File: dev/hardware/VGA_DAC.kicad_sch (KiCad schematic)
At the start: 1 part, among them J201 Conn_01x08

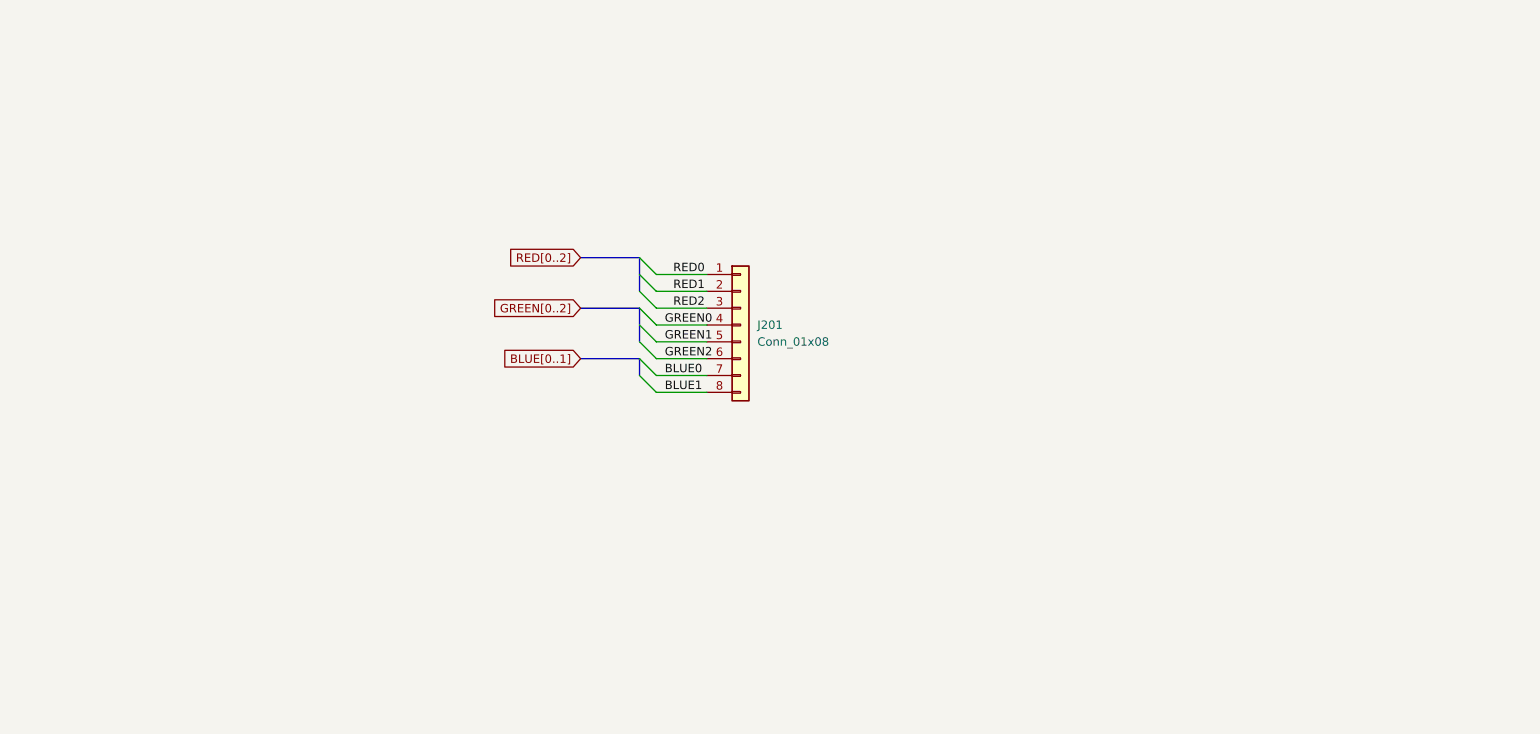
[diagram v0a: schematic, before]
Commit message: Finalized initial schematic
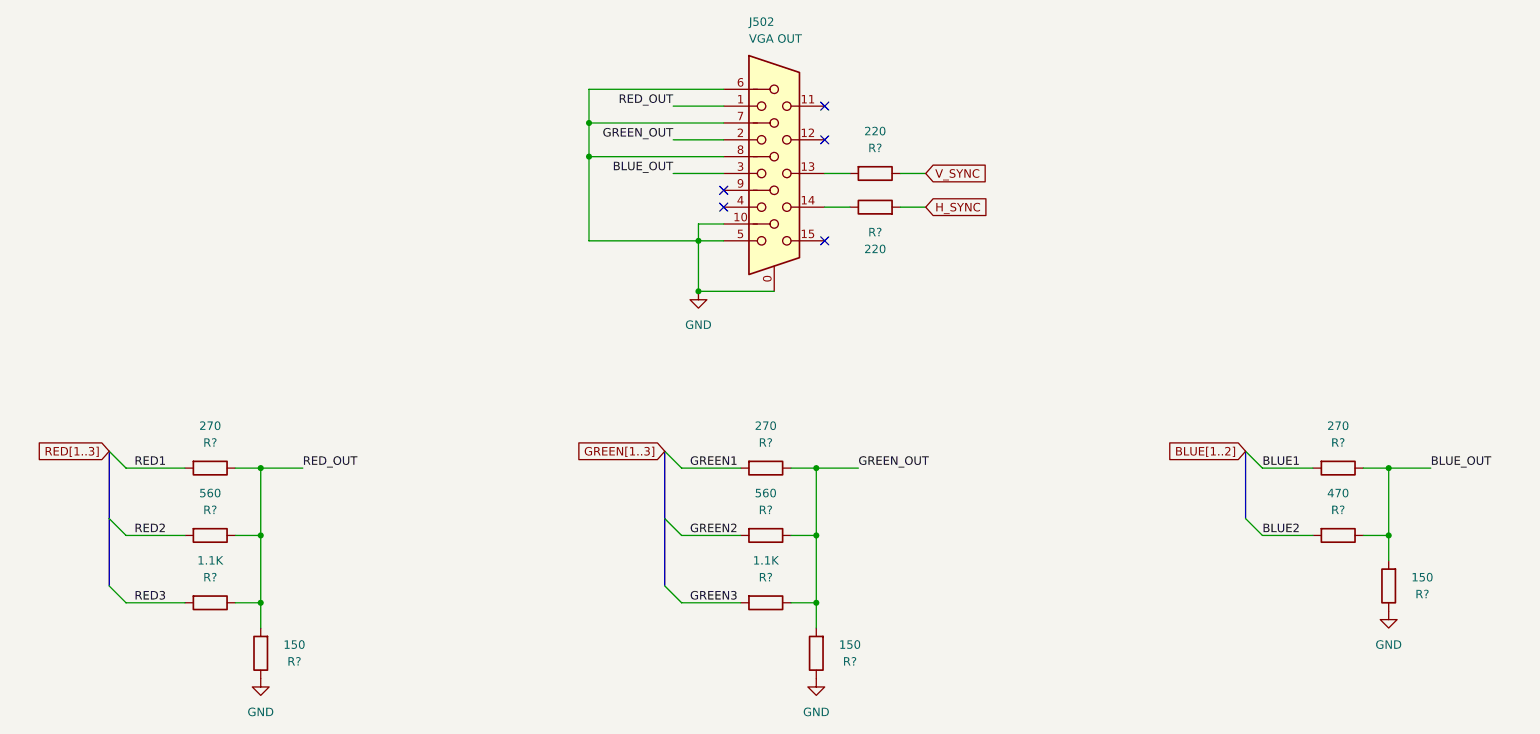
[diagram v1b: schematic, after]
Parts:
- removed J201: Conn_01x08, symbol Connector_Generic:Conn_01x08
- added J502: VGA OUT, Connector_Dsub:DSUB-15-HD_Female_Horizontal_P2.29x1.98mm_EdgePinOffset8.35mm_Housed_MountingHolesOffset10.89mm, symbol Connector:DE15_Receptacle_HighDensity_MountingHoles
- added R? (x2): 220, Resistor_THT:R_Axial_DIN0207_L6.3mm_D2.5mm_P10.16mm_Horizontal, symbol Device:R
- added R? (x2): 1.1K, Resistor_THT:R_Axial_DIN0207_L6.3mm_D2.5mm_P10.16mm_Horizontal, symbol Device:R
- added R? (x2): 560, Resistor_THT:R_Axial_DIN0207_L6.3mm_D2.5mm_P10.16mm_Horizontal, symbol Device:R
- added R?: 470, Resistor_THT:R_Axial_DIN0207_L6.3mm_D2.5mm_P10.16mm_Horizontal, symbol Device:R
- added R? (x3): 150, Resistor_THT:R_Axial_DIN0207_L6.3mm_D2.5mm_P10.16mm_Horizontal, symbol Device:R
- added R? (x3): 270, Resistor_THT:R_Axial_DIN0207_L6.3mm_D2.5mm_P10.16mm_Horizontal, symbol Device:R
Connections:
- net BLUE1: now also R?.2
- net GREEN1: now also R?.2
- net GREEN2: now also R?.2
- net RED1: now also R?.2
- net RED2: now also R?.2
- new net: J502.13, R?.2
- new net: J502.14, R?.1
- new net BLUE2: R?.2
- new net BLUE_OUT: J502.3, R?.1, R?.1, R?.2
- new net GND: J502.0, J502.10, J502.5, J502.6, J502.7, J502.8, R?.1, R?.1, R?.1
- new net GREEN3: R?.2
- new net GREEN_OUT: J502.2, R?.1, R?.1, R?.1, R?.2
- new net H_SYNC: R?.2
- new net RED3: R?.2
- new net RED_OUT: J502.1, R?.1, R?.1, R?.1, R?.2
- new net V_SYNC: R?.1
- no-connect marks 0 -> 5

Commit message: Started developing PCB layout
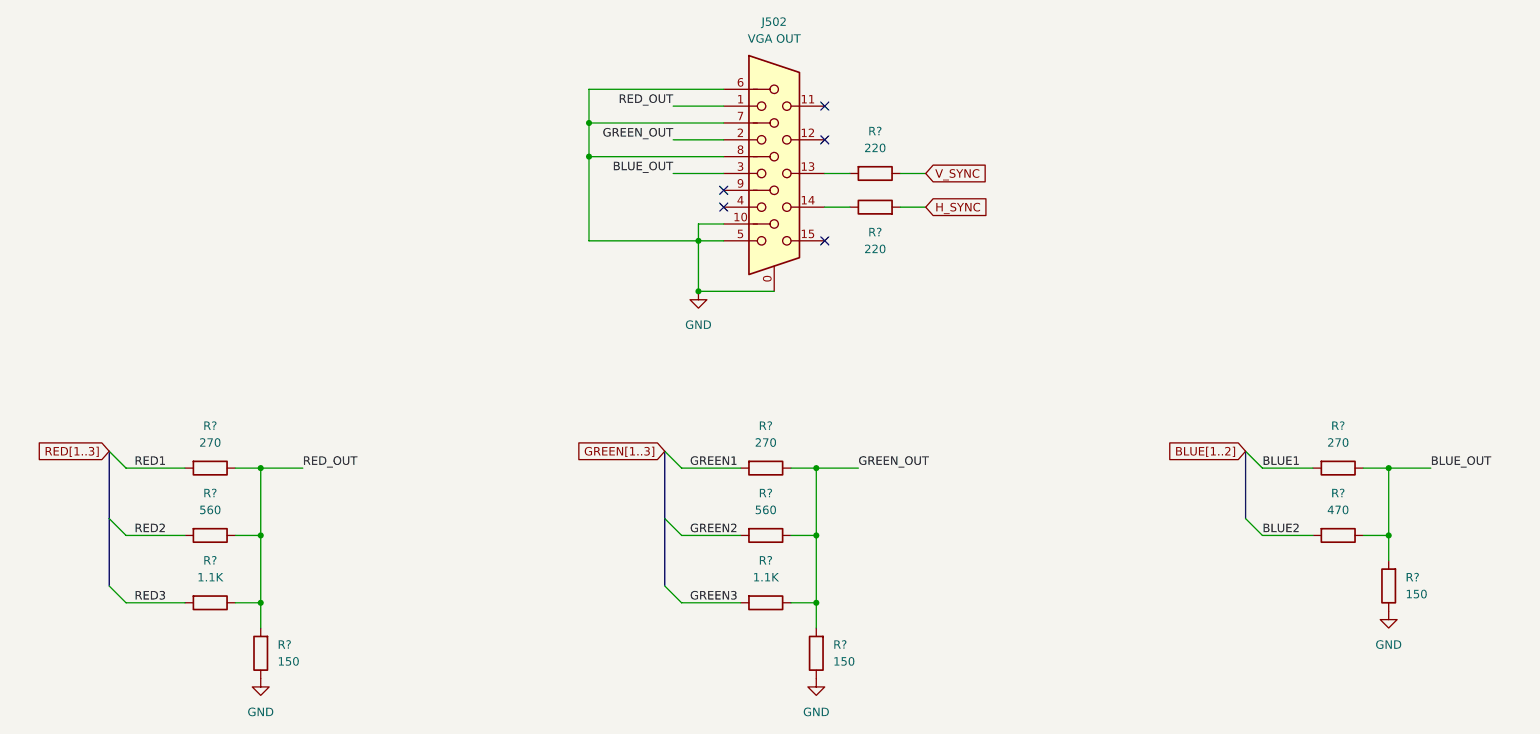
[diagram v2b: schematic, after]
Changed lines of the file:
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@@
   )
   (symbol (lib_id "Device:R") (at 161.29 63.5 270) (unit 1)
-    (in_bom yes) (on_board yes) (dnp no)
-    (property "Reference" "R?" (at 161.29 59.69 90)
-      (effects (font (size 1.27 1.27)))
-    )
-    (property "Value" "220" (at 161.29 57.15 90)
+    (in_bom yes) (on_board yes) (dnp no) (fields_autoplaced)
+    (property "Reference" "R?" (at 161.29 57.15 90)
+      (effects (font (size 1.27 1.27)))
+    )
+    (property "Value" "220" (at 161.29 59.69 90)
       (effects (font (size 1.27 1.27)))
     )
@@
   )
   (symbol (lib_id "Device:R") (at 144.78 128.27 270) (unit 1)
-    (in_bom yes) (on_board yes) (dnp no)
-    (property "Reference" "R?" (at 144.78 124.46 90)
-      (effects (font (size 1.27 1.27)))
-    )
-    (property "Value" "1.1K" (at 144.78 121.92 90)
+    (in_bom yes) (on_board yes) (dnp no) (fields_autoplaced)
+    (property "Reference" "R?" (at 144.78 121.92 90)
+      (effects (font (size 1.27 1.27)))
+    )
+    (property "Value" "1.1K" (at 144.78 124.46 90)
       (effects (font (size 1.27 1.27)))
     )
@@
   )
   (symbol (lib_id "Device:R") (at 60.96 118.11 270) (unit 1)
-    (in_bom yes) (on_board yes) (dnp no)
-    (property "Reference" "R?" (at 60.96 114.3 90)
-      (effects (font (size 1.27 1.27)))
-    )
-    (property "Value" "560" (at 60.96 111.76 90)
+    (in_bom yes) (on_board yes) (dnp no) (fields_autoplaced)
+    (property "Reference" "R?" (at 60.96 111.76 90)
+      (effects (font (size 1.27 1.27)))
+    )
+    (property "Value" "560" (at 60.96 114.3 90)
       (effects (font (size 1.27 1.27)))
     )
@@
   )
   (symbol (lib_id "Device:R") (at 231.14 118.11 270) (unit 1)
-    (in_bom yes) (on_board yes) (dnp no)
-    (property "Reference" "R?" (at 231.14 114.3 90)
-      (effects (font (size 1.27 1.27)))
-    )
-    (property "Value" "470" (at 231.14 111.76 90)
+    (in_bom yes) (on_board yes) (dnp no) (fields_autoplaced)
+    (property "Reference" "R?" (at 231.14 111.76 90)
+      (effects (font (size 1.27 1.27)))
+    )
+    (property "Value" "470" (at 231.14 114.3 90)
       (effects (font (size 1.27 1.27)))
     )
@@
   )
   (symbol (lib_id "Device:R") (at 144.78 118.11 270) (unit 1)
-    (in_bom yes) (on_board yes) (dnp no)
-    (property "Reference" "R?" (at 144.78 114.3 90)
-      (effects (font (size 1.27 1.27)))
-    )
-    (property "Value" "560" (at 144.78 111.76 90)
+    (in_bom yes) (on_board yes) (dnp no) (fields_autoplaced)
+    (property "Reference" "R?" (at 144.78 111.76 90)
+      (effects (font (size 1.27 1.27)))
+    )
+    (property "Value" "560" (at 144.78 114.3 90)
       (effects (font (size 1.27 1.27)))
     )
@@
   )
   (symbol (lib_id "Device:R") (at 161.29 68.58 90) (unit 1)
-    (in_bom yes) (on_board yes) (dnp no)
+    (in_bom yes) (on_board yes) (dnp no) (fields_autoplaced)
     (property "Reference" "R?" (at 161.29 72.39 90)
       (effects (font (size 1.27 1.27)))
@@
   )
   (symbol (lib_id "Device:R") (at 238.76 125.73 180) (unit 1)
-    (in_bom yes) (on_board yes) (dnp no)
-    (property "Reference" "R?" (at 243.84 127 0)
-      (effects (font (size 1.27 1.27)))
-    )
-    (property "Value" "150" (at 243.84 124.46 0)
-      (effects (font (size 1.27 1.27)))
+    (in_bom yes) (on_board yes) (dnp no) (fields_autoplaced)
+    (property "Reference" "R?" (at 241.3 124.46 0)
+      (effects (font (size 1.27 1.27)) (justify right))
+    )
+    (property "Value" "150" (at 241.3 127 0)
+      (effects (font (size 1.27 1.27)) (justify right))
     )
     (property "Footprint" "Resistor_THT:R_Axial_DIN0207_L6.3mm_D2.5mm_P10.16mm_Horizontal" (at 240.538 125.73 90)
@@
   )
   (symbol (lib_id "Device:R") (at 68.58 135.89 180) (unit 1)
-    (in_bom yes) (on_board yes) (dnp no)
-    (property "Reference" "R?" (at 73.66 137.16 0)
-      (effects (font (size 1.27 1.27)))
-    )
-    (property "Value" "150" (at 73.66 134.62 0)
-      (effects (font (size 1.27 1.27)))
+    (in_bom yes) (on_board yes) (dnp no) (fields_autoplaced)
+    (property "Reference" "R?" (at 71.12 134.62 0)
+      (effects (font (size 1.27 1.27)) (justify right))
+    )
+    (property "Value" "150" (at 71.12 137.16 0)
+      (effects (font (size 1.27 1.27)) (justify right))
     )
     (property "Footprint" "Resistor_THT:R_Axial_DIN0207_L6.3mm_D2.5mm_P10.16mm_Horizontal" (at 70.358 135.89 90)
@@
   )
   (symbol (lib_id "Device:R") (at 60.96 128.27 270) (unit 1)
-    (in_bom yes) (on_board yes) (dnp no)
-    (property "Reference" "R?" (at 60.96 124.46 90)
-      (effects (font (size 1.27 1.27)))
-    )
-    (property "Value" "1.1K" (at 60.96 121.92 90)
+    (in_bom yes) (on_board yes) (dnp no) (fields_autoplaced)
+    (property "Reference" "R?" (at 60.96 121.92 90)
+      (effects (font (size 1.27 1.27)))
+    )
+    (property "Value" "1.1K" (at 60.96 124.46 90)
       (effects (font (size 1.27 1.27)))
     )
@@
   )
   (symbol (lib_id "Device:R") (at 231.14 107.95 270) (unit 1)
-    (in_bom yes) (on_board yes) (dnp no)
-    (property "Reference" "R?" (at 231.14 104.14 90)
-      (effects (font (size 1.27 1.27)))
-    )
-    (property "Value" "270" (at 231.14 101.6 90)
+    (in_bom yes) (on_board yes) (dnp no) (fields_autoplaced)
+    (property "Reference" "R?" (at 231.14 101.6 90)
+      (effects (font (size 1.27 1.27)))
+    )
+    (property "Value" "270" (at 231.14 104.14 90)
       (effects (font (size 1.27 1.27)))
     )
@@
   )
   (symbol (lib_id "Device:R") (at 152.4 135.89 180) (unit 1)
-    (in_bom yes) (on_board yes) (dnp no)
-    (property "Reference" "R?" (at 157.48 137.16 0)
-      (effects (font (size 1.27 1.27)))
-    )
-    (property "Value" "150" (at 157.48 134.62 0)
-      (effects (font (size 1.27 1.27)))
+    (in_bom yes) (on_board yes) (dnp no) (fields_autoplaced)
+    (property "Reference" "R?" (at 154.94 134.62 0)
+      (effects (font (size 1.27 1.27)) (justify right))
+    )
+    (property "Value" "150" (at 154.94 137.16 0)
+      (effects (font (size 1.27 1.27)) (justify right))
     )
     (property "Footprint" "Resistor_THT:R_Axial_DIN0207_L6.3mm_D2.5mm_P10.16mm_Horizontal" (at 154.178 135.89 90)
@@
   )
   (symbol (lib_id "Connector:DE15_Receptacle_HighDensity_MountingHoles") (at 146.05 63.5 0) (unit 1)
-    (in_bom yes) (on_board yes) (dnp no)
-    (property "Reference" "J502" (at 142.24 40.64 0)
-      (effects (font (size 1.27 1.27)) (justify left))
-    )
-    (property "Value" "VGA OUT" (at 142.24 43.18 0)
-      (effects (font (size 1.27 1.27)) (justify left))
+    (in_bom yes) (on_board yes) (dnp no) (fields_autoplaced)
+    (property "Reference" "J502" (at 146.05 40.64 0)
+      (effects (font (size 1.27 1.27)))
+    )
+    (property "Value" "VGA OUT" (at 146.05 43.18 0)
+      (effects (font (size 1.27 1.27)))
     )
     (property "Footprint" "Connector_Dsub:DSUB-15-HD_Female_Horizontal_P2.29x1.98mm_EdgePinOffset8.35mm_Housed_MountingHolesOffset10.89mm" (at 121.92 53.34 0)
@@
   )
   (symbol (lib_id "Device:R") (at 144.78 107.95 270) (unit 1)
-    (in_bom yes) (on_board yes) (dnp no)
-    (property "Reference" "R?" (at 144.78 104.14 90)
-      (effects (font (size 1.27 1.27)))
-    )
-    (property "Value" "270" (at 144.78 101.6 90)
+    (in_bom yes) (on_board yes) (dnp no) (fields_autoplaced)
+    (property "Reference" "R?" (at 144.78 101.6 90)
+      (effects (font (size 1.27 1.27)))
+    )
+    (property "Value" "270" (at 144.78 104.14 90)
       (effects (font (size 1.27 1.27)))
     )
@@
   )
   (symbol (lib_id "Device:R") (at 60.96 107.95 270) (unit 1)
-    (in_bom yes) (on_board yes) (dnp no)
-    (property "Reference" "R?" (at 60.96 104.14 90)
-      (effects (font (size 1.27 1.27)))
-    )
-    (property "Value" "270" (at 60.96 101.6 90)
-      (effects (font (size 1.27 1.27)))
-    )
+    (in_bom yes) (on_board yes) (dnp no) (fields_autoplaced)
+    (property "Reference" "R?" (at 60.96 101.6 90)
+      (effects (font (size 1.27 1.27)))
+    )
+    (property "Value" "270" (at 60.96 104.14 90)
+      (effects (font (size 1.27 1.27)))
+    )

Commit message: Thicc-traced VGA sig test - REVERT HERE
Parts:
- removed R? (x2): 1.1K, Resistor_THT:R_Axial_DIN0207_L6.3mm_D2.5mm_P10.16mm_Horizontal, symbol Device:R
- removed R? (x2): 560, Resistor_THT:R_Axial_DIN0207_L6.3mm_D2.5mm_P10.16mm_Horizontal, symbol Device:R
- removed R?: 470, Resistor_THT:R_Axial_DIN0207_L6.3mm_D2.5mm_P10.16mm_Horizontal, symbol Device:R
- removed R? (x3): 150, Resistor_THT:R_Axial_DIN0207_L6.3mm_D2.5mm_P10.16mm_Horizontal, symbol Device:R
- removed R? (x3): 270, Resistor_THT:R_Axial_DIN0207_L6.3mm_D2.5mm_P10.16mm_Horizontal, symbol Device:R
- added R? (x8): 309, Resistor_THT:R_Axial_DIN0207_L6.3mm_D2.5mm_P10.16mm_Horizontal, symbol Device:R
- added R? (x2): 146, Resistor_THT:R_Axial_DIN0207_L6.3mm_D2.5mm_P10.16mm_Horizontal, symbol Device:R
- added R? (x4): 154, Resistor_THT:R_Axial_DIN0207_L6.3mm_D2.5mm_P10.16mm_Horizontal, symbol Device:R
- added R? (x3): 266, Resistor_THT:R_Axial_DIN0207_L6.3mm_D2.5mm_P10.16mm_Horizontal, symbol Device:R
- added R?: 133, Resistor_THT:R_Axial_DIN0207_L6.3mm_D2.5mm_P10.16mm_Horizontal, symbol Device:R
- added R?: 173, Resistor_THT:R_Axial_DIN0207_L6.3mm_D2.5mm_P10.16mm_Horizontal, symbol Device:R
- renumbered J502 to J501
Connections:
- net BLUE1: now also R?.2
- net BLUE2: now also R?.2
- net BLUE_OUT: now also R?.1, R?.1, R?.2
- net GND: now also R?.1, R?.1, R?.1, R?.2, R?.2, R?.2
- net GREEN1: now also R?.2
- net GREEN2: now also R?.2
- net GREEN3: now also R?.2
- net GREEN_OUT: now also R?.1, R?.1, R?.2
- net RED1: now also R?.2
- net RED2: now also R?.2
- net RED3: now also R?.2
- net RED_OUT: now also R?.1, R?.1, R?.2
- new net: R?.1, R?.1, R?.2 (x5)

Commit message: Finalized dev board administrivia
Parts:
- removed R? (x7): 309, Resistor_THT:R_Axial_DIN0207_L6.3mm_D2.5mm_P10.16mm_Horizontal, symbol Device:R
- removed R?: 146, Resistor_THT:R_Axial_DIN0207_L6.3mm_D2.5mm_P10.16mm_Horizontal, symbol Device:R
- removed R? (x3): 154, Resistor_THT:R_Axial_DIN0207_L6.3mm_D2.5mm_P10.16mm_Horizontal, symbol Device:R
- removed R?: 220, Resistor_THT:R_Axial_DIN0207_L6.3mm_D2.5mm_P10.16mm_Horizontal, symbol Device:R
- removed R? (x2): 266, Resistor_THT:R_Axial_DIN0207_L6.3mm_D2.5mm_P10.16mm_Horizontal, symbol Device:R
- added R? (x7): 309, Resistor_THT:R_Axial_DIN0207_L6.3mm_D2.5mm_P10.16mm_Horizontal, symbol Device:R
- added R? (x2): 267, Resistor_THT:R_Axial_DIN0207_L6.3mm_D2.5mm_P10.16mm_Horizontal, symbol Device:R
- added R? (x3): 154, Resistor_THT:R_Axial_DIN0207_L6.3mm_D2.5mm_P10.16mm_Horizontal, symbol Device:R
- added R?: 147, Resistor_THT:R_Axial_DIN0207_L6.3mm_D2.5mm_P10.16mm_Horizontal, symbol Device:R
- added R?: 220, Resistor_THT:R_Axial_DIN0207_L6.3mm_D2.5mm_P10.16mm_Horizontal, symbol Device:R
- J501: footprint Connector_Dsub:DSUB-15-HD_Female_Horizontal_P2.29x1.98mm_EdgePinOffset8.35mm_Housed_MountingHolesOffset10.89mm -> jcap-footprints:2311763-2; Part (none) -> 2311763-2
- R?: Part (none) -> MFR-25FRF52-220R
- R?: Part (none) -> MFR-25FBF52-133R
- R?: Part (none) -> SFR16S0003090FR500
- R?: value 266 -> 267; Part (none) -> RNF14FTD267R
- R?: value 173 -> 174; Part (none) -> MFR-25FRF52-174R
- R?: value 146 -> 147; Part (none) -> MFR-25FBF52-147R
- R?: Part (none) -> MFR-25FBF52-154R
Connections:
- net BLUE2: now also R?.2
- net GND: now also R?.1, R?.2, R?.2, R?.2
- net GREEN1: now also R?.2
- net GREEN2: now also R?.2
- net GREEN3: now also R?.2
- net GREEN_OUT: now also R?.1, R?.1, R?.2
- net H_SYNC: now also R?.1
- net RED2: now also R?.2
- net RED3: now also R?.2
- net at R?.2: now also R?.1, R?.1 (x2)
- net at J501.14: now also R?.2
- new net: R?.1, R?.1, R?.2 (x3)
